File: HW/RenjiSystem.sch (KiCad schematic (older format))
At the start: 14 parts, among them J1 Screw_Terminal_AC100VHOT, J2 Screw_Terminal_AC100VCOLD, J3 Screw_Terminal_UV_HOT, J4 Screw_Terminal_UV_COLD, J5 Screw_Terminal_HEATER_HOT, J6 Screw_Terminal_HEATER_COLD, J7 Screw_Terminal_FAN_HOT, J8 Screw_Terminal_FAN_COLD

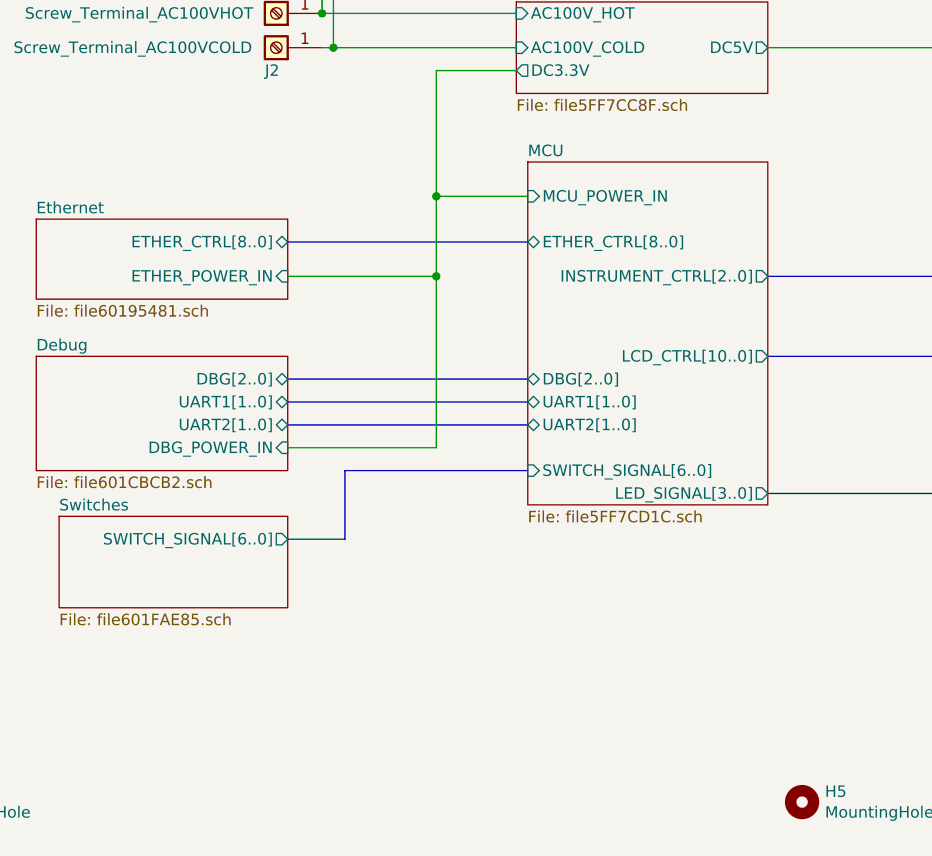
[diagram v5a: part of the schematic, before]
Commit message: シルクで1ピンマーク追記
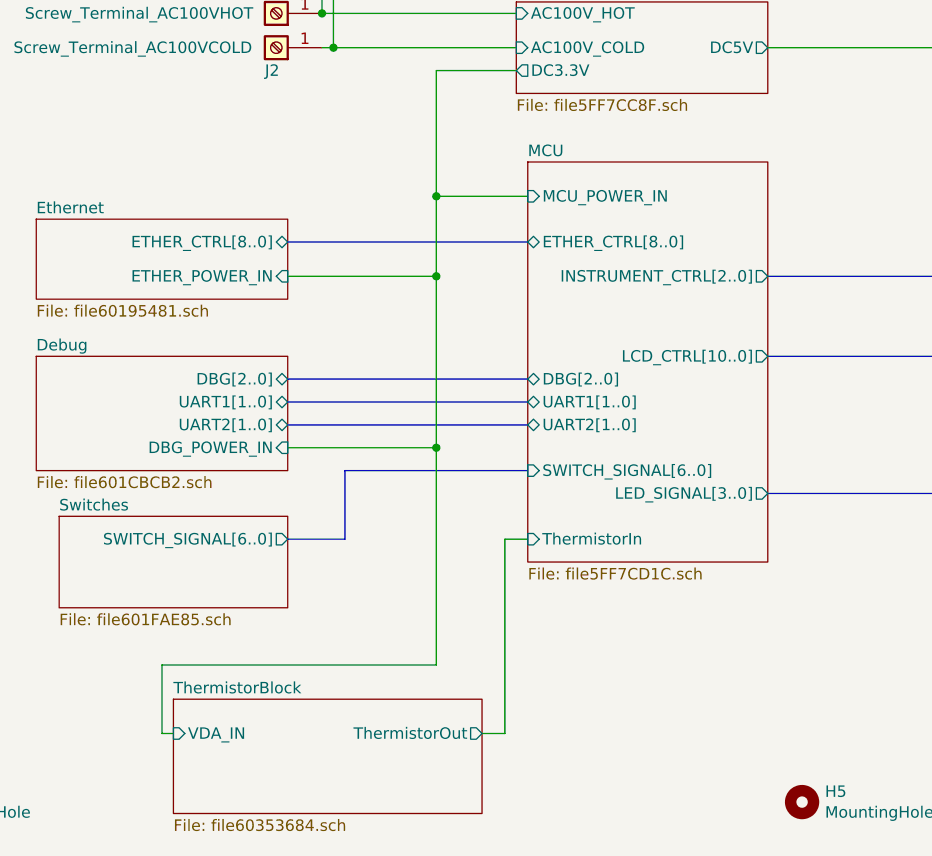
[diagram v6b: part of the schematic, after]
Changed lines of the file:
@@
 $Descr A4 11693 8268
 encoding utf-8
-Sheet 1 9
+Sheet 1 10
 Title ""
 Date ""
@@
 $EndSheet
 $Sheet
-S 4050 2500 1050 1500
+S 4050 2500 1050 1750
 U 5FF7CD1D
 F0 "MCU" 50
@@
 F9 "SWITCH_SIGNAL[6..0]" I L 4050 3850 50
 F10 "LED_SIGNAL[3..0]" O R 5100 3950 50
+F11 "ThermistorIn" I L 4050 4150 50
 $EndSheet
 $Sheet
@@
 	3000 3000 3650 3000
 Connection ~ 3650 3000
-Wire Wire Line
-	3650 3000 3650 3750
 Wire Bus Line
 	3000 3450 4050 3450
@@
 	1    0    0    -1
 $EndComp
+$Sheet
+S 2500 4850 1350 500
+U 60353685
+F0 "ThermistorBlock" 50
+F1 "file60353684.sch" 50
+F2 "VDA_IN" I L 2500 5000 50
+F3 "ThermistorOut" O R 3850 5000 50
+$EndSheet
+Wire Wire Line
+	3650 4700 2450 4700
+Wire Wire Line
+	2450 4700 2450 5000
+Wire Wire Line
+	2450 5000 2500 5000
+Wire Wire Line
+	3650 3000 3650 3750
+Connection ~ 3650 3750
+Wire Wire Line
+	3650 3750 3650 4700
+Wire Wire Line
+	3850 5000 3950 5000
+Wire Wire Line
+	3950 5000 3950 4150
+Wire Wire Line
+	3950 4150 4050 4150
 $EndSCHEMATC
